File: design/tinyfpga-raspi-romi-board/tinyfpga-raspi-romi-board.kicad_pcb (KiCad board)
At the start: 2 copper layers, 103.4 x 121.3 mm, 72 parts, among them J1 TINYFPGA_J1, J10 ROMI_ENC_LEFT, J11 ROMI_ENC_RIGHT, J12 QTR_LEFT, J13 QTR_RIGHT, J14 SONAR_LEFT, J15 SONAR_RIGHT, J16 PWR_SEL1, J17 PWR_SEL0, J18 RPI_EXTRA, J19 ON_OFF, J2 TINYFPGA_J2, J20 ROMI_POWER, J3 Raspberry_Pi_2_3, J4 TINYFPGA_J4, J5 TINYFPGA_J5, J6 WP_JUMP, J7 ROMI_VSW, J8 FUSE_JUMP, J9 ROMI_MOTOR_DRIVE, Q1 2N7000, Q2 2N7000, Q3 2N7000, Q4 2N7000, Q5 2N7000, Q6 2N7000, Q7 2N7000, Q8 2N7000, SW2 SW_Push, SW3 SW_Push, SW4 SW_Push, U1 CAT24C128

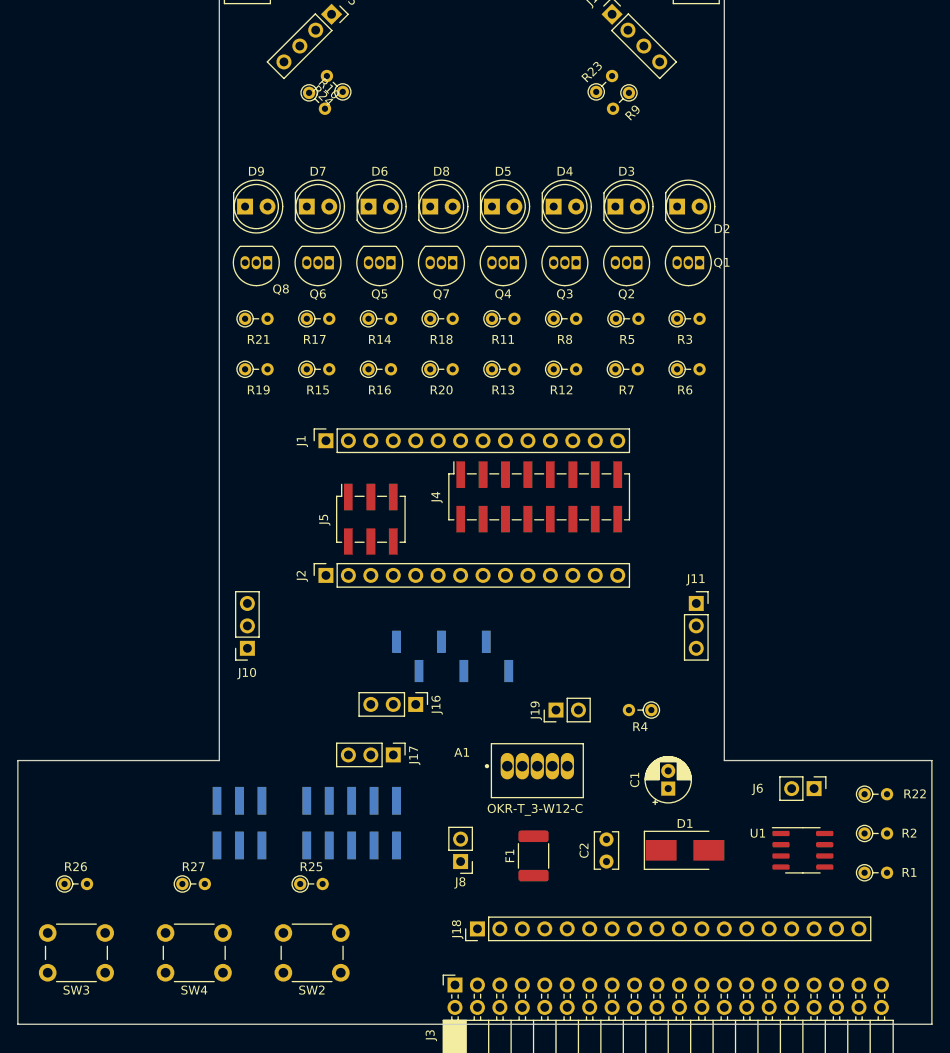
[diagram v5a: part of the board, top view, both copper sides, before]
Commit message: oh hey look its all through hole
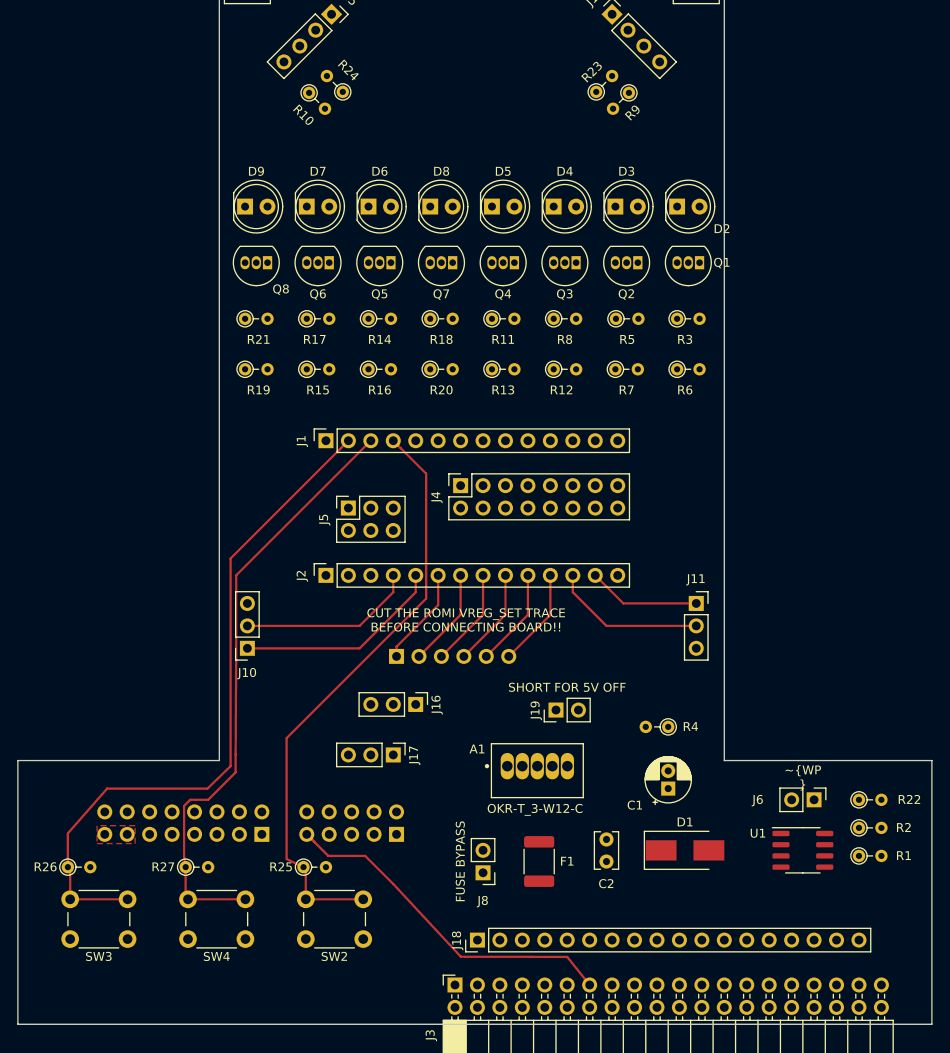
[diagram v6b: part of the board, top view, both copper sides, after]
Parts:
- J20: footprint Connector_PinHeader_2.54mm:PinHeader_2x05_P2.54mm_Vertical_SMD -> Connector_PinHeader_2.54mm:PinHeader_2x05_P2.54mm_Vertical
- J4: footprint Connector_PinSocket_2.54mm:PinSocket_2x08_P2.54mm_Vertical_SMD -> Connector_PinSocket_2.54mm:PinSocket_2x08_P2.54mm_Vertical
- J5: footprint Connector_PinSocket_2.54mm:PinSocket_2x03_P2.54mm_Vertical_SMD -> Connector_PinSocket_2.54mm:PinSocket_2x03_P2.54mm_Vertical
- J7: footprint Connector_PinHeader_2.54mm:PinHeader_2x03_P2.54mm_Vertical_SMD -> Connector_PinHeader_2.54mm:PinHeader_2x08_P2.54mm_Vertical
- J9: footprint Connector_PinHeader_2.54mm:PinHeader_1x06_P2.54mm_Vertical_SMD_Pin1Left -> Connector_PinHeader_2.54mm:PinHeader_1x06_P2.54mm_Vertical
- moved J4 8.98 mm to (102.9, 88.3)
- moved J9 6.35 mm to (95.6, 107.6)
- moved J20 5.24 mm to (95.6, 127.7), turned to 90 degrees
- moved SW4 4.58 mm to (78.5, 139.6)
- moved SW2 4.58 mm to (91.9, 139.6)
- moved SW3 4.58 mm to (65.2, 139.6)
- moved J8 2.84 mm to (105.4, 132.1)
- moved J5 2.84 mm to (90.2, 90.8)
- moved J7 2.84 mm to (80.4, 127.7)
- moved R4 2.69 mm to (126.4, 115.6)
- moved R1 2.01 mm to (148.0, 130.2)
- moved R26 1.94 mm to (58.4, 131.4)
- moved R25 1.94 mm to (85.1, 131.4)
- moved R27 1.94 mm to (71.8, 131.4)
- moved J6 1.27 mm to (142.9, 123.8)
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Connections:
- A1 pad 2: Net-(A1-Pad2) -> +BATT
- A1 pad 4: (no net) -> Net-(A1-Pad4)
- F1 pad 2: Net-(A1-Pad2) -> Net-(A1-Pad4)
- J18 pad 17: /RPI_GPIO26 -> (no net)
- J18 pad 18: /RPI_GPIO27 -> (no net)
- J2 pad 10: /ROMI_PWMR -> /ROMI_DIRR
- J2 pad 11: /ROMI_ENC_LA -> /ROMI_PWMR
- J2 pad 12: /ROMI_ENC_LB -> /ROMI_ENC_RB
- J2 pad 14: /ROMI_ENC_RB -> /FPGA_LED0
- J2 pad 4: /FPGA_LED0 -> /ROMI_ENC_LB
- J2 pad 5: /ROMI_~SLPL -> /ROMI_ENC_LA
- J2 pad 6: /ROMI_DIRL -> /ROMI_~SLPL
- J2 pad 7: /ROMI_PWML -> /ROMI_DIRL
- J2 pad 8: /ROMI_~SLPR -> /ROMI_PWML
- J2 pad 9: /ROMI_DIRR -> /ROMI_~SLPR
- J20 pad 1: /RPI_GPIO26 -> /ROMI_3V3
- J20 pad 3: /RPI_GPIO24 -> /ROMI_3V3
- J20 pad 7: /ROMI_3V3 -> /ROMI_PG
- J20 pad 9: /ROMI_3V3 -> /ROMI_SHDN
- J3 pad 13: /RPI_GPIO27 -> /ROMI_SHDN
- J3 pad 37: /RPI_GPIO26 -> /ROMI_PG
- J8 pad 2: Net-(A1-Pad2) -> Net-(A1-Pad4)
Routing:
- net /FPGA_BTN0: track 0.00 -> 78.2 mm
- net /FPGA_BTN1: track 0.00 -> 68.4 mm
- net /FPGA_BTN_RST: track 0.00 -> 67.8 mm
- net /ROMI_SHDN: track 0.00 -> 40.7 mm
- net /ROMI_ENC_LA: track 0.00 -> 23.6 mm
- net /ROMI_ENC_LB: track 0.00 -> 20.0 mm
- net /ROMI_ENC_RB: track 0.00 -> 17.5 mm
- net /ROMI_ENC_RA: track 0.00 -> 12.7 mm
- net /ROMI_~SLPR: track 0.00 -> 11.1 mm
- net /ROMI_PWMR: track 0.00 -> 11.1 mm
- net /ROMI_DIRL: track 0.00 -> 11.1 mm
- net /ROMI_~SLPL: track 0.00 -> 11.1 mm
- net /ROMI_PWML: track 0.00 -> 11.1 mm
- net /ROMI_DIRR: track 0.00 -> 11.1 mm
- added copper zone on F.Cu, net Net-(J7-Pad13)
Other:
- board text added: "CUT THE ROMI VREG_SET TRACE BEFORE CONNECTING BOARD!!"
- board text added: "FUSE BYPASS"
- board text added: "SHORT FOR 5V OFF"
- board text added: "~WP"

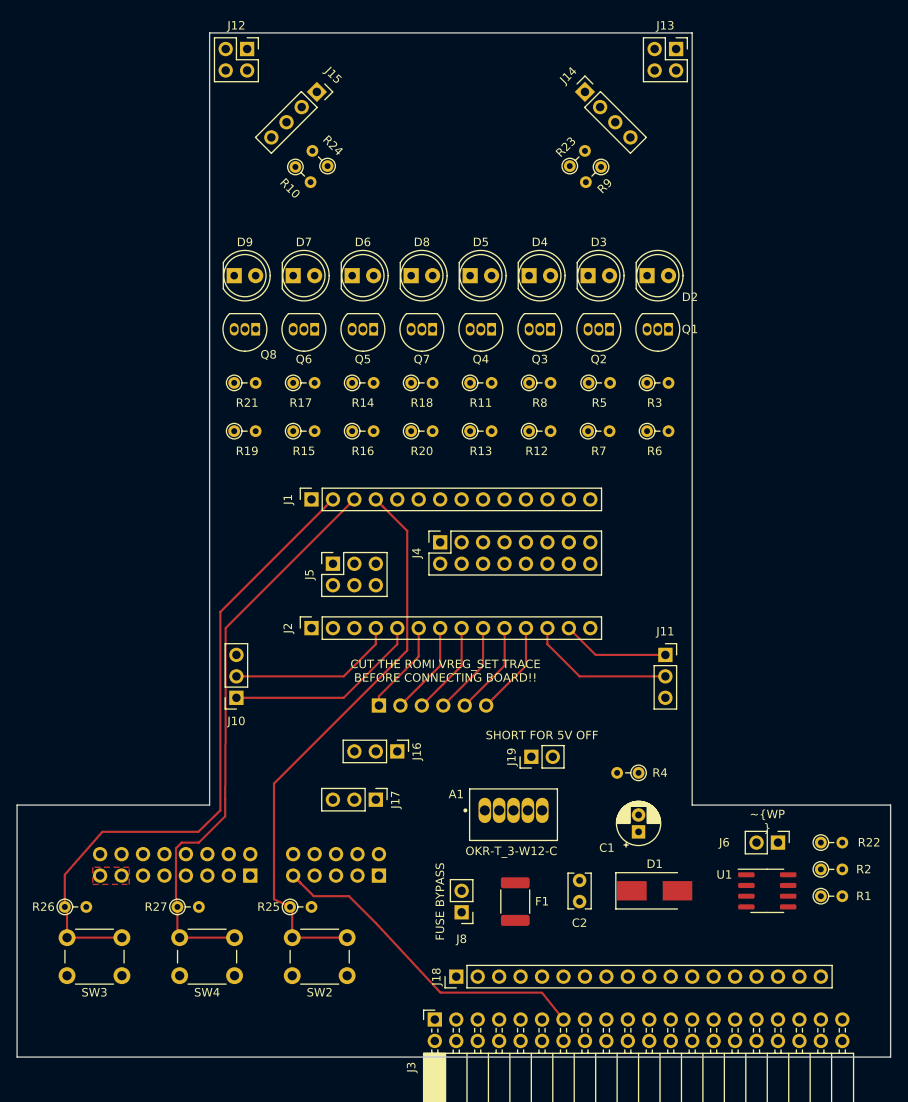
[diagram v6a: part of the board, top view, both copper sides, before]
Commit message: updated mechanical dimensions, moved power and buttons
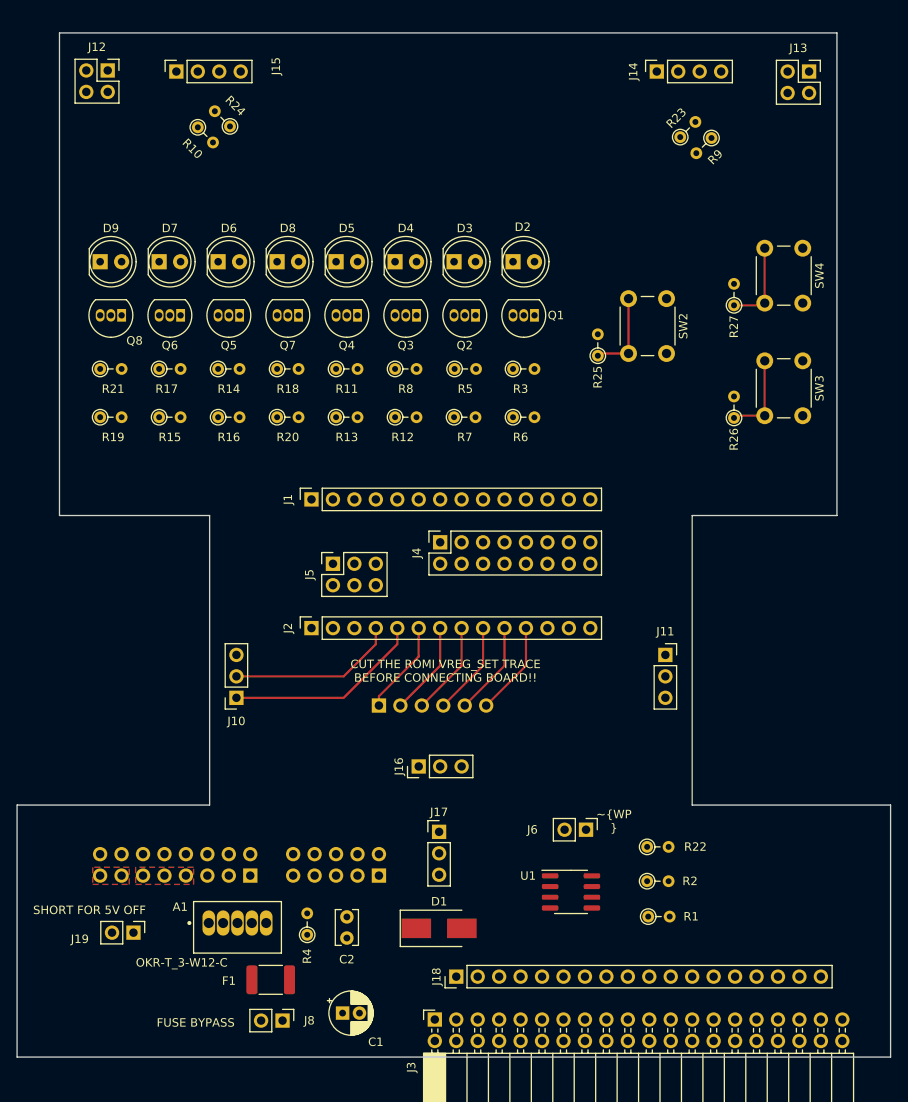
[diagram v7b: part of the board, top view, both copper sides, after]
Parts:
- moved SW4 109.3 mm to (145.8, 53.4), turned to 270 degrees
- moved SW3 108.6 mm to (145.8, 66.8), turned to 270 degrees
- moved R26 98.2 mm to (137.7, 73.5), turned to 90 degrees
- moved R27 97.1 mm to (137.7, 60.2), turned to 90 degrees
- moved SW2 88.7 mm to (129.7, 59.4), turned to 270 degrees
- moved R25 74.8 mm to (121.5, 66.2), turned to 90 degrees
- moved J19 51.5 mm to (66.5, 134.5), turned to 270 degrees
- moved R4 43.7 mm to (87.1, 134.7), turned to 90 degrees
- moved C1 41.1 mm to (91.3, 144.0), turned to 0 degrees
- moved A1 35.3 mm to (78.9, 133.3)
- moved F1 30.4 mm to (82.8, 140.1), turned to 180 degrees
- moved C2 27.9 mm to (91.8, 135.1)
- moved D1 25.9 mm to (102.7, 134.0)
- moved J8 24.8 mm to (84.2, 144.9), turned to 270 degrees
- moved U1 23.2 mm to (118.4, 129.7)
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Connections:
- J1 pad 1: GND -> +5V
- J1 pad 2: /FPGA_BTN0 -> GND
- J1 pad 3: /FPGA_BTN1 -> /FPGA_3.3V_OUT
- J2 pad 1: +5V -> GND
- J2 pad 2: GND -> /FPGA_BTN0
- J2 pad 3: /FPGA_3.3V_OUT -> /FPGA_BTN1
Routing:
- net /FPGA_BTN0: track 78.2 -> 10.2 mm
- net /FPGA_BTN1: track 68.4 -> 10.2 mm
- net /FPGA_BTN_RST: track 67.8 -> 10.2 mm
- net /ROMI_SHDN: track 40.7 -> 0.00 mm
- net /ROMI_ENC_RB: track 17.5 -> 0.00 mm
- net /ROMI_ENC_RA: track 12.7 -> 0.00 mm
- added copper zone on F.Cu, net Net-(J7-Pad11)
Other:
- outline, holes or cut-outs redrawn
